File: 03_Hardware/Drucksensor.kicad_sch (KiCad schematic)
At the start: 94 parts, among them J101 24V in, J103 RS485-mini-1, J104 RJ45, J108 RJ45, J109 RJ45, J110 DS18B20, J111 BMP280, J112 RJ45, J113 RS485-mini-1, J114 AVR-ISP-6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

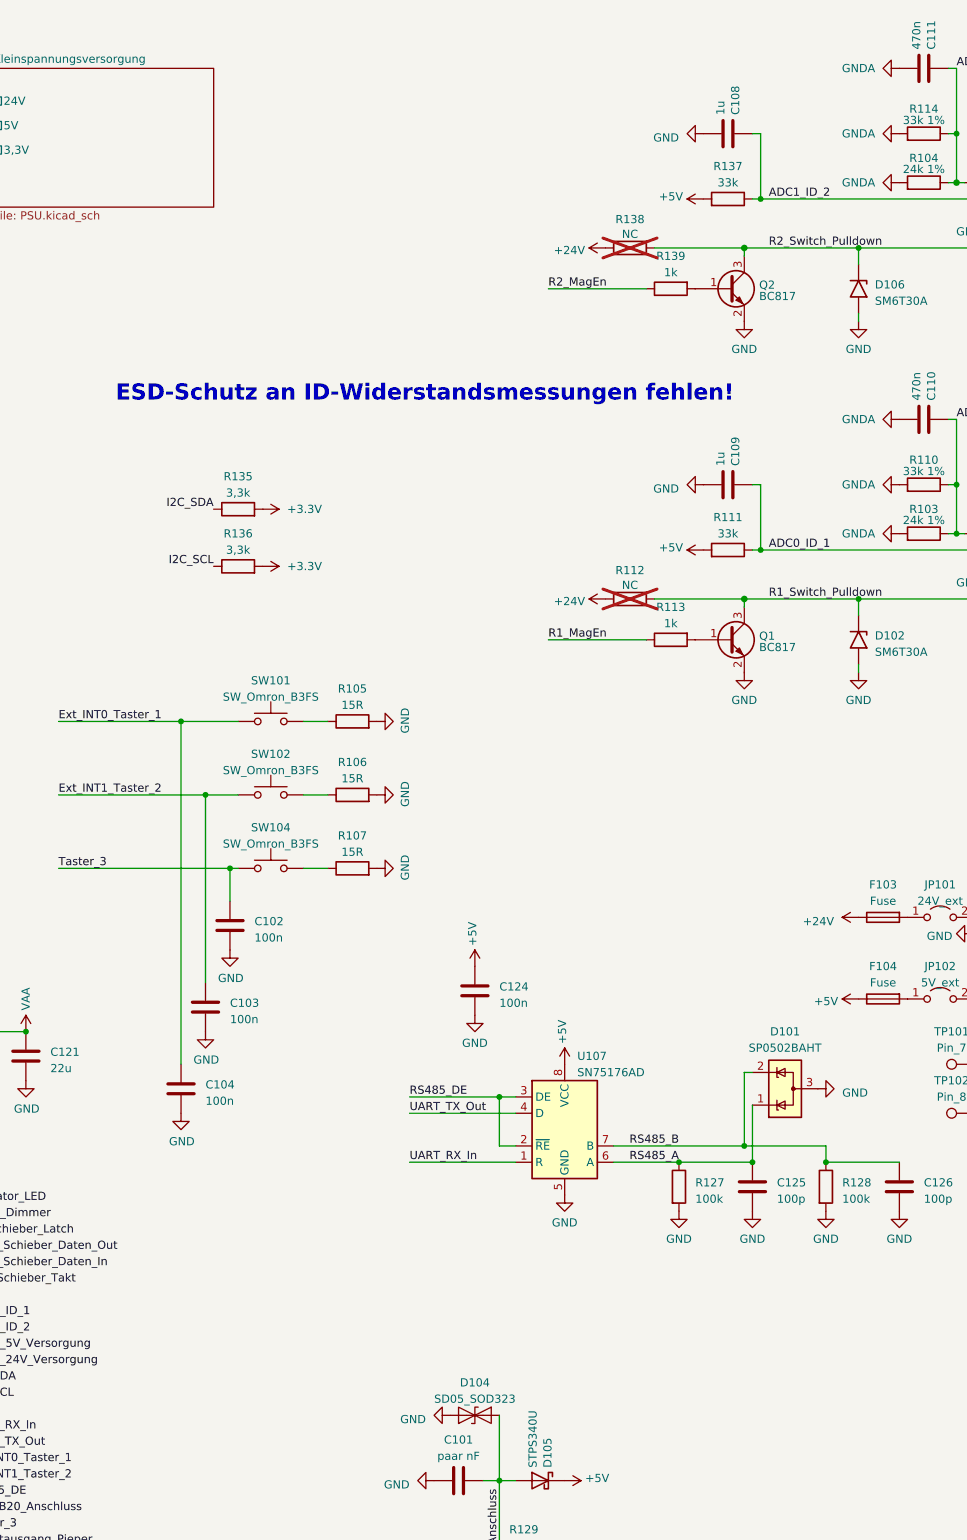
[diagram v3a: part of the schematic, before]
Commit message: Folgende Änderungen wurden gelöscht und erneut durchgeführt UniDir 5V TVS Diode an ID Leitung Sensor angebracht Spannungsteiler Detektion Sensor => 18k
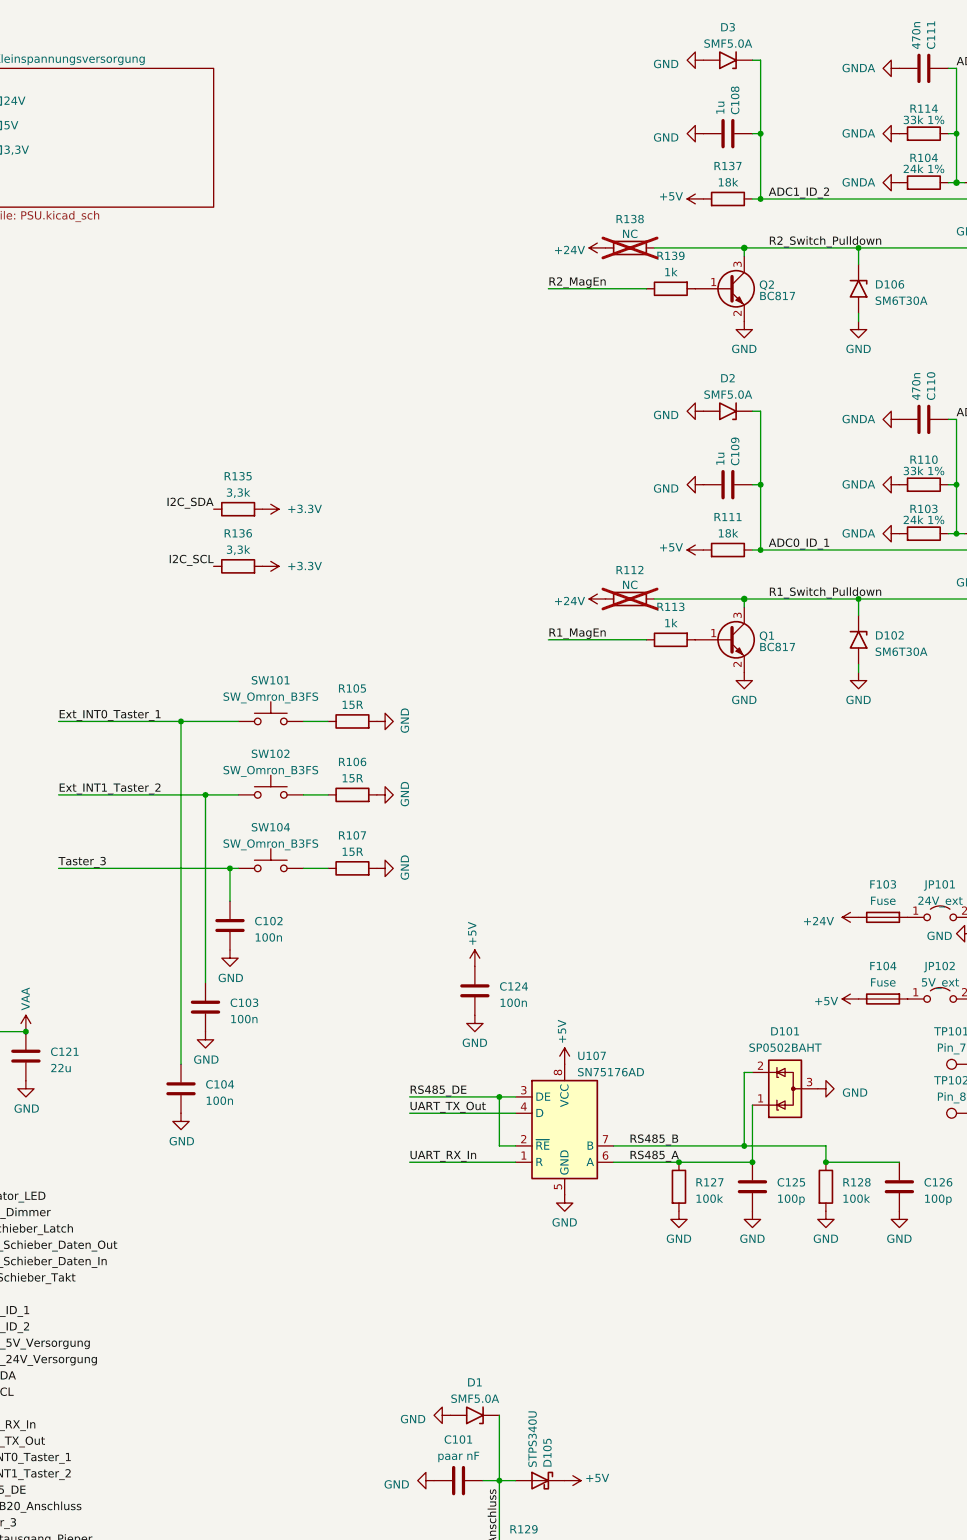
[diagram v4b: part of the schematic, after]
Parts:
- removed D104: SD05_SOD323, Diode_SMD:D_SOD-323, symbol Diode:SD05_SOD323
- added D1, D2, D3: SMF5.0A, Diode_SMD:D_SOD-123F, symbol Diode:SM6T30A
- R111, R137: value 33k -> 18k
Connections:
- net ADC0_ID_1: now also D2.1 (A1)
- net ADC1_ID_2: now also D3.1 (A1)
- net DS18B20_Anschluss: now also D1.1 (A1)
- net GND: now also D1.2 (A2), D2.2 (A2), D3.2 (A2)
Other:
- note removed: "ESD-Schutz an ID-Widerstandsmessungen fehlen!"
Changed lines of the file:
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@@
   (junction (at 120.65 72.39) (diameter 0) (color 0 0 0 0)
   )
+  (junction (at 317.5 90.17) (diameter 0) (color 0 0 0 0)
+  )
   (junction (at 231.14 138.43) (diameter 0) (color 0 0 0 0)
   )
@@
   (junction (at 189.23 175.26) (diameter 0) (color 0 0 0 0)
   )
+  (junction (at 317.5 35.56) (diameter 0) (color 0 0 0 0)
+  )
   (junction (at 130.81 217.17) (diameter 0) (color 0 0 0 0)
   )
@@
     (stroke (width 0) (type solid))
   )
+  (wire (pts (xy 317.5 24.13) (xy 317.5 35.56))
+    (stroke (width 0) (type default))
+  )
   (wire (pts (xy 356.87 172.72) (xy 368.3 172.72))
     (stroke (width 0) (type default))
@@
     (stroke (width 0) (type solid))
   )
+  (wire (pts (xy 316.23 24.13) (xy 317.5 24.13))
+    (stroke (width 0) (type default))
+  )
   (wire (pts (xy 316.23 35.56) (xy 317.5 35.56))
     (stroke (width 0) (type default))
@@
     (stroke (width 0) (type default))
   )
+  (wire (pts (xy 317.5 78.74) (xy 317.5 90.17))
+    (stroke (width 0) (type default))
+  )
   (wire (pts (xy 184.15 175.26) (xy 189.23 175.26))
     (stroke (width 0) (type default))
@@
     (stroke (width 0) (type default))
   )
+  (wire (pts (xy 316.23 78.74) (xy 317.5 78.74))
+    (stroke (width 0) (type default))
+  )
   (wire (pts (xy 350.52 170.18) (xy 369.57 170.18))
     (stroke (width 0) (type default))
@@
     (stroke (width 0) (type default))
   )
-  (text "ESD-Schutz an ID-Widerstandsmessungen fehlen!" (at 217.17 77.47 0)
-    (effects (font (size 2.5 2.5) (thickness 0.5) bold (color 221 38 8 1)) (justify left bottom))
-  )
   (text "Messröhre ADC:\nVon Röhre 0-10V\nTeiler 20k:13.895k (33.895k R-ges)\nErgibt Teilerverhältnis von 0,40995\nBei idealem Teilerverhältnis von 0,4096\n"
     (at 361.95 124.46 0)
@@
     )
   )
+  (symbol (lib_id "Diode:SM6T30A") (at 273.05 234.95 180) (unit 1)
+    (in_bom yes) (on_board yes) (dnp no) (fields_autoplaced)
+    (property "Reference" "D1" (at 273.05 229.87 0)
+      (effects (font (size 1.27 1.27)))
+    )
+    (property "Value" "SMF5.0A" (at 273.05 232.41 0)
+      (effects (font (size 1.27 1.27)))
+    )
+    (property "Footprint" "Diode_SMD:D_SOD-123F" (at 273.05 229.87 0)
+      (effects (font (size 1.27 1.27)) hide)
+    )
+    (property "Datasheet" "" (at 274.32 234.95 0)
+      (effects (font (size 1.27 1.27)) hide)
+    )
+    (property "Arrow" "" (at 273.05 234.95 0)
+      (effects (font (size 1.27 1.27)))
+    )
+    (property "LedColor" "" (at 273.05 234.95 0)
+      (effects (font (size 1.27 1.27)))
+    )
+    (pin "1")
+    (pin "2")
+    (instances
+      (project "Drucksensor"
+        (path "/d772951a-27ae-4d3f-b561-d53c012cef6f"
+          (reference "D1") (unit 1)
+        )
+      )
+    )
+  )
   (symbol (lib_id "power:+24V") (at 368.3 38.1 90) (mirror x) (unit 1)
     (in_bom yes) (on_board yes) (dnp no)
@@
     )
   )
+  (symbol (lib_id "Diode:SM6T30A") (at 312.42 78.74 180) (unit 1)
+    (in_bom yes) (on_board yes) (dnp no) (fields_autoplaced)
+    (property "Reference" "D2" (at 312.42 73.66 0)
+      (effects (font (size 1.27 1.27)))
+    )
+    (property "Value" "SMF5.0A" (at 312.42 76.2 0)
+      (effects (font (size 1.27 1.27)))
+    )
+    (property "Footprint" "Diode_SMD:D_SOD-123F" (at 312.42 73.66 0)
+      (effects (font (size 1.27 1.27)) hide)
+    )
+    (property "Datasheet" "" (at 313.69 78.74 0)
+      (effects (font (size 1.27 1.27)) hide)
+    )
+    (property "Arrow" "" (at 312.42 78.74 0)
+      (effects (font (size 1.27 1.27)))
+    )
+    (property "LedColor" "" (at 312.42 78.74 0)
+      (effects (font (size 1.27 1.27)))
+    )
+    (pin "1")
+    (pin "2")
+    (instances
+      (project "Drucksensor"
+        (path "/d772951a-27ae-4d3f-b561-d53c012cef6f"
+          (reference "D2") (unit 1)
+        )
+      )
+    )
+  )
   (symbol (lib_id "Connector:TestPoint") (at 350.52 180.34 90) (unit 1)
     (in_bom yes) (on_board yes) (dnp no) (fields_autoplaced)
@@
     )
   )
-  (symbol (lib_id "Diode:SD05_SOD323") (at 273.05 234.95 0) (unit 1)
-    (in_bom yes) (on_board yes) (dnp no) (fields_autoplaced)
-    (property "Reference" "D104" (at 273.05 229.87 0)
-      (effects (font (size 1.27 1.27)))
-    )
-    (property "Value" "SD05_SOD323" (at 273.05 232.41 0)
-      (effects (font (size 1.27 1.27)))
-    )
-    (property "Footprint" "Diode_SMD:D_SOD-323" (at 273.05 240.03 0)
-      (effects (font (size 1.27 1.27)) hide)
-    )
-    (property "Datasheet" "https://www.littelfuse.com/~/media/electronics/datasheets/tvs_diode_arrays/littelfuse_tvs_diode_array_sd_c_datasheet.pdf.pdf" (at 273.05 234.95 0)
-      (effects (font (size 1.27 1.27)) hide)
-    )
-    (pin "1")
-    (pin "2")
-    (instances
-      (project "Drucksensor"
-        (path "/d772951a-27ae-4d3f-b561-d53c012cef6f"
-          (reference "D104") (unit 1)
-        )
-      )
-    )
-  )
   (symbol (lib_id "power:GND") (at 172.72 148.59 0) (unit 1)
     (in_bom yes) (on_board yes) (dnp no)
@@
       (effects (font (size 1.27 1.27)))
     )
-    (property "Value" "33k" (at 312.42 43.18 90)
+    (property "Value" "18k" (at 312.42 43.18 90)
       (effects (font (size 1.27 1.27)))
     )
@@
     )
   )
+  (symbol (lib_id "power:GND") (at 308.61 24.13 270) (unit 1)
+    (in_bom yes) (on_board yes) (dnp no) (fields_autoplaced)
+    (property "Reference" "#PWR02" (at 302.26 24.13 0)
+      (effects (font (size 1.27 1.27)) hide)
+    )
+    (property "Value" "GND" (at 304.8 24.765 90)
+      (effects (font (size 1.27 1.27)) (justify right))
+    )
+    (property "Footprint" "" (at 308.61 24.13 0)
+      (effects (font (size 1.27 1.27)) hide)
+    )
+    (property "Datasheet" "" (at 308.61 24.13 0)
+      (effects (font (size 1.27 1.27)) hide)
+    )
+    (pin "1")
+    (instances
+      (project "Drucksensor"
+        (path "/d772951a-27ae-4d3f-b561-d53c012cef6f"
+          (reference "#PWR02") (unit 1)
+        )
+      )
+    )
+  )
   (symbol (lib_id "power:GND") (at 241.3 262.89 270) (unit 1)
     (in_bom yes) (on_board yes) (dnp no)
@@
       (effects (font (size 1.27 1.27)))
     )
-    (property "Value" "33k" (at 312.42 97.79 90)
+    (property "Value" "18k" (at 312.42 97.79 90)
       (effects (font (size 1.27 1.27)))
     )
@@
     )
   )
+  (symbol (lib_id "power:GND") (at 308.61 78.74 270) (unit 1)
+    (in_bom yes) (on_board yes) (dnp no) (fields_autoplaced)
+    (property "Reference" "#PWR01" (at 302.26 78.74 0)
+      (effects (font (size 1.27 1.27)) hide)
+    )
+    (property "Value" "GND" (at 304.8 79.375 90)
+      (effects (font (size 1.27 1.27)) (justify right))
+    )
+    (property "Footprint" "" (at 308.61 78.74 0)
+      (effects (font (size 1.27 1.27)) hide)
+    )
+    (property "Datasheet" "" (at 308.61 78.74 0)
+      (effects (font (size 1.27 1.27)) hide)
+    )
+    (pin "1")
+    (instances
+      (project "Drucksensor"
+        (path "/d772951a-27ae-4d3f-b561-d53c012cef6f"
+          (reference "#PWR01") (unit 1)
+        )
+      )
+    )
+  )
   (symbol (lib_id "power:GND") (at 81.28 90.17 90) (unit 1)
     (in_bom yes) (on_board yes) (dnp no)
@@
         )
       )
+    )
+  )
+  (symbol (lib_id "Diode:SM6T30A") (at 312.42 24.13 180) (unit 1)
+    (in_bom yes) (on_board yes) (dnp no) (fields_autoplaced)
+    (property "Reference" "D3" (at 312.42 19.05 0)
+      (effects (font (size 1.27 1.27)))
+    )
+    (property "Value" "SMF5.0A" (at 312.42 21.59 0)
+      (effects (font (size 1.27 1.27)))
+    )
+    (property "Footprint" "Diode_SMD:D_SOD-123F" (at 312.42 19.05 0)
+      (effects (font (size 1.27 1.27)) hide)
+    )
+    (property "Datasheet" "" (at 313.69 24.13 0)
+      (effects (font (size 1.27 1.27)) hide)
+    )
+    (property "Arrow" "" (at 312.42 24.13 0)
+      (effects (font (size 1.27 1.27)))
+    )
+    (property "LedColor" "" (at 312.42 24.13 0)
+      (effects (font (size 1.27 1.27)))
+    )
+    (pin "1")
+    (pin "2")
+    (instances
+      (project "Drucksensor"
+        (path "/d772951a-27ae-4d3f-b561-d53c012cef6f"
+          (reference "D3") (unit 1)
+        )
+      )

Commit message: Layout weitergemacht, RJ45 Buchsen fehlen noch komplett
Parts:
- SW103: footprint (none) -> Button_Switch_THT:SW_DIP_SPSTx08_Slide_9.78x22.5mm_W7.62mm_P2.54mm
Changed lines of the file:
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@@
     (comment 1 "Philipp Hörauf")
     (comment 2 "Sven Schneider")
+    (comment 3 "David Palm")
   )
   (junction (at 120.65 69.85) (diameter 0) (color 0 0 0 0)
@@
       (effects (font (size 1.27 1.27)))
     )
-    (property "Footprint" "" (at 111.76 69.85 0)
+    (property "Footprint" "Button_Switch_THT:SW_DIP_SPSTx08_Slide_9.78x22.5mm_W7.62mm_P2.54mm" (at 111.76 69.85 0)
       (effects (font (size 1.27 1.27)) hide)
     )
